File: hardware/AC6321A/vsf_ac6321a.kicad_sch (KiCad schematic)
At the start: 29 parts, among them J1 Conn_02x15_Odd_Even, J2 USB_C_Receptacle_USB2.0, J3 USB_C_Receptacle_USB2.0, J4 USB_A, J5 Conn_01x02, U2 CH340N, Y1 24M, +-10PPM,12pF

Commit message: [hardware/AC6321A] update
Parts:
- added JP1, JP2, JP3, JP4: Jumper_2_Open, VSF:SolderJumper-2_P0.8mm_Open_Pad0.6x0.8mm, symbol Jumper:Jumper_2_Open
- added Q1, Q3: S8050, Package_TO_SOT_SMD:TSOT-23, symbol Transistor_BJT:Q_NPN_BEC
- added Q2, Q4: LPM9013, Package_TO_SOT_SMD:SOT-23, symbol Transistor_FET:Q_PMOS_GSD
- added R10, R11, R4, R5: 100K, Resistor_SMD:R_0402_1005Metric, symbol Device:R
- added SW1: SW_Push, VSF:JHA004, symbol Switch:SW_Push
- J5: footprint (none) -> Connector_PinHeader_2.54mm:PinHeader_1x02_P2.54mm_Vertical
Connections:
- net PWR_3V3 is gone; now on net VCORE: J1.27 (Pin_27)
- net GND: now also C4.1, C5.1, C6.1, C7.1, C8.1, C9.1, Q1.2 (E), Q3.2 (E), SW1.1
- net USB5V: now also JP2.2 (B), JP4.1 (A), Q4.3 (D); no longer D1.2 (A2), J2.A4 (VBUS), J2.A9 (VBUS), J2.B4 (VBUS), J2.B9 (VBUS), J3.A4 (VBUS), J3.A9 (VBUS), J3.B4 (VBUS), J3.B9 (VBUS), J4.1 (VBUS), U2.5 (VCC)
- net USB5V_OUT: now also J4.1 (VBUS), JP2.1 (A)
- net VBAT: now also JP3.1 (A), Q2.3 (D); no longer BT1.1 (+)
- net PWREN renamed RST
- net RST: now also Q1.1 (B), Q3.1 (B), R10.2, R5.2, SW1.2
- new net: BT1.1 (+), JP3.2 (B), Q2.2 (S), R4.1, R5.1
- new net: Q1.3 (C), Q4.1 (G), R11.2
- new net: Q2.1 (G), Q3.3 (C), R4.2
- new net USB5V_IN: J2.A4 (VBUS), J2.A9 (VBUS), J2.B4 (VBUS), J2.B9 (VBUS), JP1.1 (A), JP4.2 (B), Q4.2 (S), R10.1, R11.1
- new net USB5V_USART: D1.2 (A2), J3.A4 (VBUS), J3.A9 (VBUS), J3.B4 (VBUS), J3.B9 (VBUS), JP1.2 (B), U2.5 (VCC)
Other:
- moved on the sheet: AE1, BT1, C10, C4, C5, C6, C7, C8, C9, J1, J4, L1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

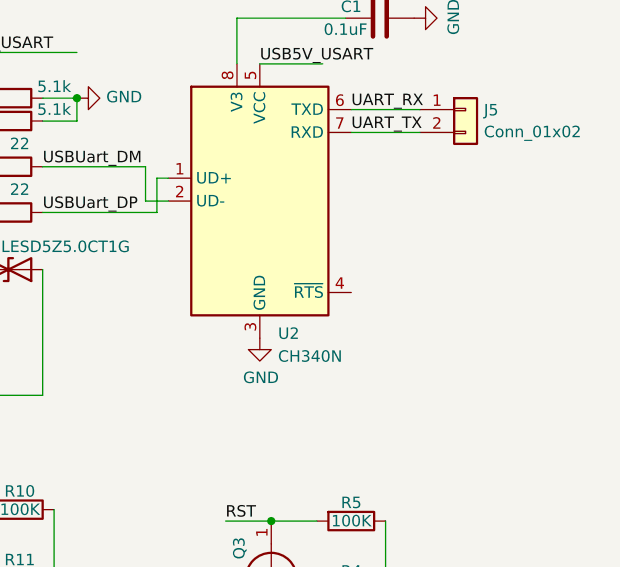
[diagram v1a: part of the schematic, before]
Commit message: [hardware/AC6321A] RST can be controlled by RTS in CH340N
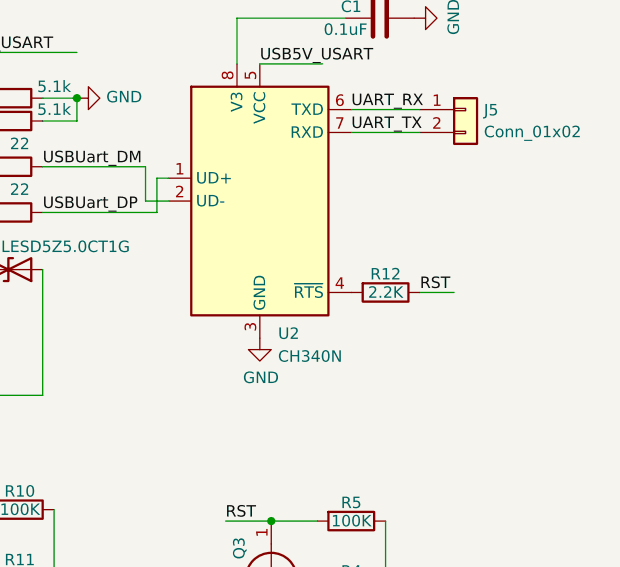
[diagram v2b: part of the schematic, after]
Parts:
- added R12: 2.2K, Resistor_SMD:R_0402_1005Metric, symbol Device:R
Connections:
- net RST: now also R12.1
- net at U2.4 (~{RTS}): now also R12.2
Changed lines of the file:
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@@
+	(wire
+		(pts
+			(xy 266.7 54.61) (xy 270.51 54.61)
+		)
+		(stroke
+			(width 0)
+			(type default)
+		)
+	)
 	(wire
 		(pts
@@
 	(label "USB5V_IN"
 		(at 151.13 27.94 0)
+		(effects
+			(font
+				(size 1.27 1.27)
+			)
+			(justify left bottom)
+		)
+	)
+	(label "RST"
+		(at 266.7 54.61 0)
 		(effects
 			(font
@@
 					(unit 1)
 				)
+			)
+		)
+	)
+	(symbol
+		(lib_id "Device:R")
+		(at 262.89 54.61 270)
+		(unit 1)
+		(exclude_from_sim no)
+		(in_bom yes)
+		(on_board yes)
+		(dnp no)
+		(property "Reference" "R12"
+			(at 262.89 52.578 90)
+			(effects
+				(font
+					(size 1.27 1.27)
+				)
+			)
+		)
+		(property "Value" "2.2K"
+			(at 262.89 54.61 90)
+			(effects
+				(font
+					(size 1.27 1.27)
+				)
+			)
+		)
+		(property "Footprint" "Resistor_SMD:R_0402_1005Metric"
+			(at 262.89 52.832 90)
+			(effects
+				(font
+					(size 1.27 1.27)
+				)
+				(hide yes)
+			)
+		)
+		(property "Datasheet" "~"
+			(at 262.89 54.61 0)
+			(effects
+				(font
+					(size 1.27 1.27)
+				)
+				(hide yes)
+			)
+		)
+		(property "Description" "Resistor"
+			(at 262.89 54.61 0)
+			(effects
+				(font
+					(size 1.27 1.27)
+				)
+				(hide yes)
+			)
+		)
+		(pin "1"
+		)
+		(pin "2"
+		)
+		(instances
+			(project "vsf_ac6321a"
+				(path "/b1f641fc-4d4b-41df-b1cf-71a1edbad872"
+					(reference "R12")
+					(unit 1)
+				)
